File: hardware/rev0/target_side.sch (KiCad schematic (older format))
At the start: 4 parts, among them IC1 ECP5-BGA256, U9 AT86RF215

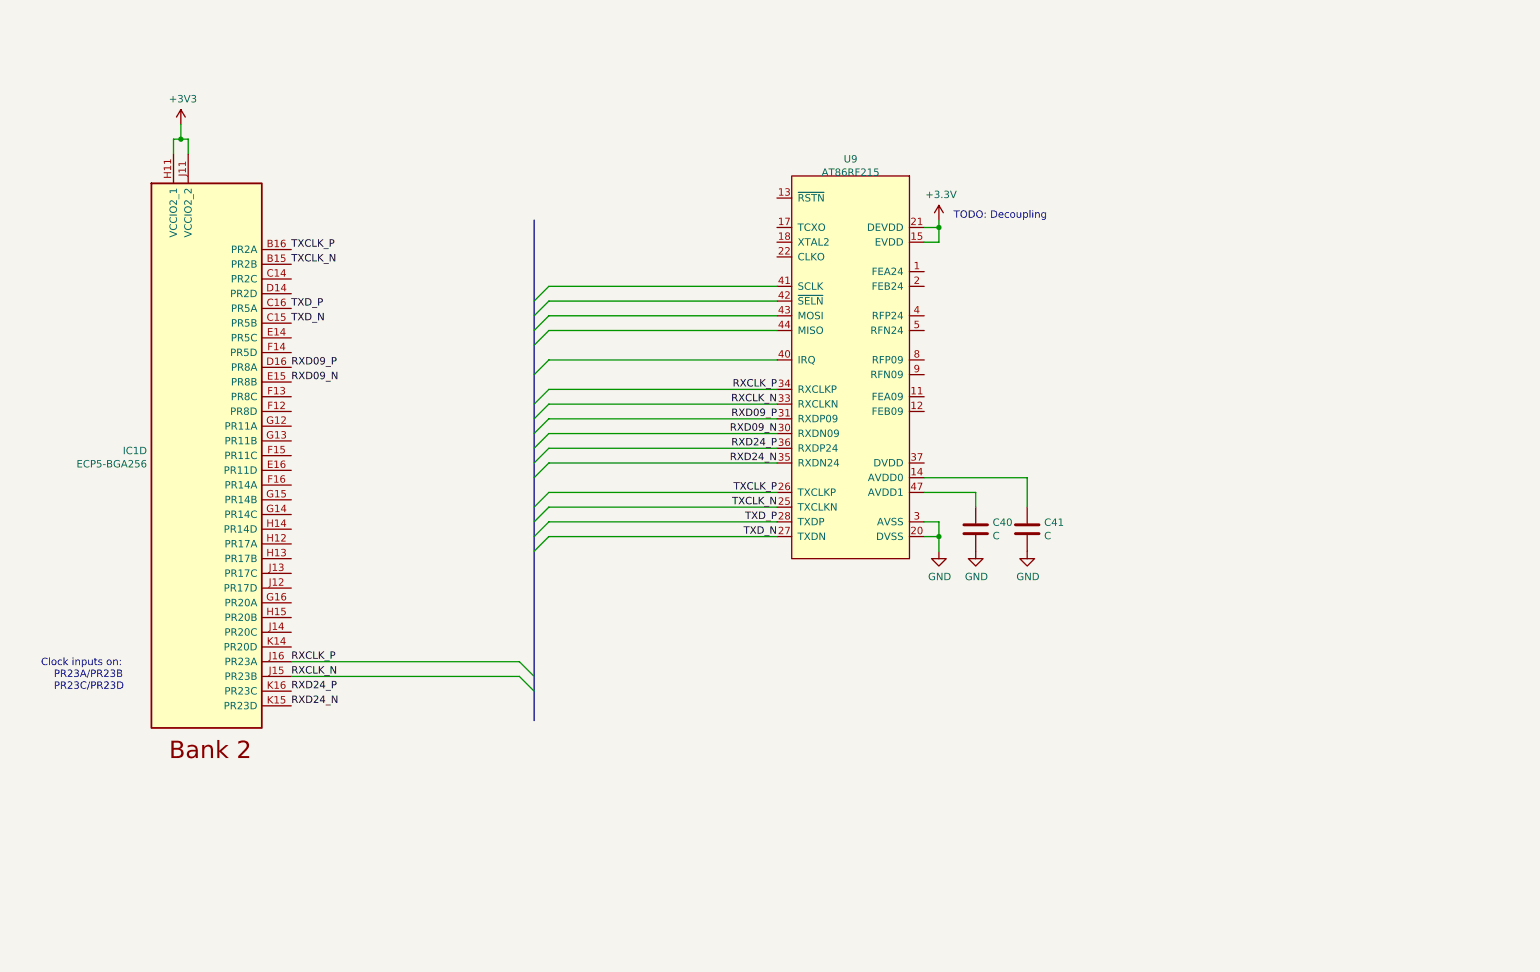
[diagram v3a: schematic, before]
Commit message: Add baluns, matching, TXCO, decoupling
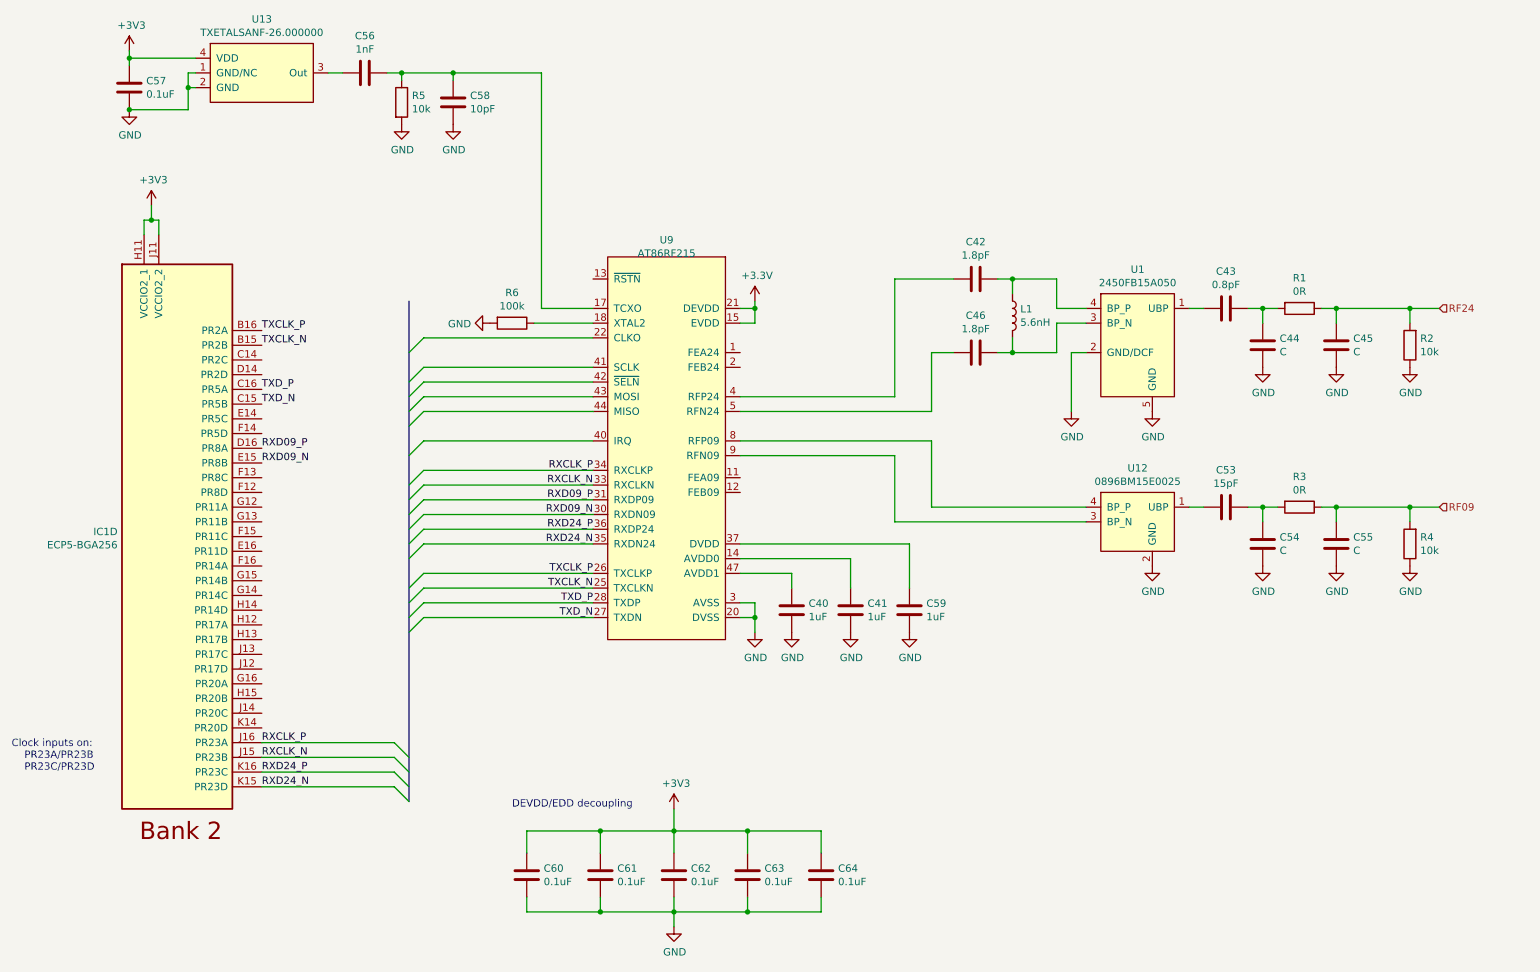
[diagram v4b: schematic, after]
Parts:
- added C42, C46: 1.8pF, Capacitor_SMD:C_0402_1005Metric, symbol Device:C
- added C43: 0.8pF, Capacitor_SMD:C_0402_1005Metric, symbol Device:C
- added C44, C45, C54, C55: C, Capacitor_SMD:C_0402_1005Metric, symbol Device:C
- added C53: 15pF, Capacitor_SMD:C_0402_1005Metric, symbol Device:C
- added C56: 1nF, Capacitor_SMD:C_0402_1005Metric, symbol Device:C
- added C57, C60, C61, C62, C63, C64: 0.1uF, Capacitor_SMD:C_0402_1005Metric, symbol Device:C
- added C58: 10pF, Capacitor_SMD:C_0402_1005Metric, symbol Device:C
- added C59: 1uF, Capacitor_SMD:C_0402_1005Metric, symbol Device:C
- added L1: 5.6nH, Inductor_SMD:L_0402_1005Metric, symbol Device:L
- added R1, R3: 0R, Resistor_SMD:R_0402_1005Metric, symbol Device:R
- added R2, R4, R5: 10k, Resistor_SMD:R_0402_1005Metric, symbol Device:R
- added R6: 100k, Resistor_SMD:R_0402_1005Metric, symbol Device:R
- added U1: 2450FB15A050, amalthea:Filter_Johanson_2x1.25mm, symbol rf:2450FB15A050
- added U12: 0896BM15E0025, amalthea:Filter_Johanson_2x1.25mm, symbol rf:0896BM15E0025
- added U13: TXETALSANF-26.000000, Oscillator:Oscillator_SMD_SeikoEpson_SG8002CE-4Pin_3.2x2.5mm, symbol rf:TXETALSANF-26.000000
- C40, C41: value C -> 1uF; footprint (none) -> Capacitor_SMD:C_0402_1005Metric
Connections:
- net +3V3: now also C57.1, C60.1, C61.1, C62.1, C63.1, C64.1, U13.4 (VDD)
- net AVSS: now also C44.2, C45.2, C54.2, C55.2, C57.2, C58.2, C59.2, C60.2, C61.2, C62.2, C63.2, C64.2, R2.1, R4.1, R5.2, R6.2, U1.2 (GND/DCF), U1.5 (GND), U12.2 (GND), U12.5 (GND), U12.6 (GND), U13.1 (GND/NC), U13.2 (GND)
- net at U9.17 (TCXO): now also C56.1, C58.1, R5.1
- net at U9.18 (XTAL2): now also R6.1
- net at U9.37 (DVDD): now also C59.1
- net at U9.4 (RFP24): now also C42.2
- net at U9.5 (RFN24): now also C46.1
- net at U9.8 (RFP09): now also U12.4 (BP_P)
- net at U9.9 (RFN09): now also U12.3 (BP_N)
- new net: C43.2, U1.1 (UBP)
- new net: C46.2, L1.2, U1.3 (BP_N)
- new net: C42.1, L1.1, U1.4 (BP_P)
- new net: C53.2, U12.1 (UBP)
- new net: C43.1, C44.1, R1.2
- new net: C53.1, C54.1, R3.2
- new net: C56.2, U13.3 (Out)
- new net RF09: C55.1, R3.1, R4.2
- new net RF24: C45.1, R1.1, R2.2
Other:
- note added: "DEVDD/EDD decoupling"
- note removed: "TODO: Decoupling\n"
- moved on the sheet: C40, C41, IC1D, U9

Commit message: Do a bunch of placement
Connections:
- net ~SELN: now reaches IC1.E16 (PR11D)
- net ~SELN: now also U9.42 (~SELN)
- net MOSI: now reaches IC1.F16 (PR14A)
- net MOSI: now also U9.43 (MOSI)
- net MISO: now reaches IC1.G16 (PR20A)
- net MISO: now also U9.44 (MISO)
- net SCLK: now reaches IC1.K14 (PR20D)
- net SCLK: now also U9.41 (SCLK)
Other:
- note added: "TODO: swap 24/09 position to match physical layout"
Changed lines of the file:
@@
 U 1 1 5E8BDF16
 P 5150 3900
-F 0 "U9" H 5150 5315 50  0000 C CNN
-F 1 "AT86RF215" H 5150 5224 50  0000 C CNN
+F 0 "U9" H 5150 5350 50  0000 C CNN
+F 1 "AT86RF215" H 5150 5250 50  0000 C CNN
 F 2 "Package_DFN_QFN:QFN-48-1EP_7x7mm_P0.5mm_EP5.6x5.6mm" H 5150 3650 50  0001 C CNN
 F 3 "" H 5150 3650 50  0001 C CNN
@@
 Wire Wire Line
 	6700 4400 8000 4400
-Text HLabel 10400 4300 2    50   Input ~ 0
-RF09
 $Comp
 L Device:C C42
@@
 	-1   0    0    1
 $EndComp
-Text HLabel 10400 2950 2    50   Input ~ 0
-RF24
 Wire Wire Line
 	9100 2950 9200 2950
@@
 Wire Wire Line
 	5700 6500 6200 6500
+Text Notes 4100 6350 0    50   ~ 0
+DEVDD/EDD decoupling
+Text Label 4650 3350 2    50   ~ 0
+SCLK
+Text Label 4650 3450 2    50   ~ 0
+~SELN
+Text Label 4650 3550 2    50   ~ 0
+MOSI
+Text Label 4650 3650 2    50   ~ 0
+MISO
 Wire Bus Line
 	3400 2900 3400 6300
-Text Notes 4100 6350 0    50   ~ 0
-DEVDD/EDD decoupling
+Text Notes 8550 2500 0    50   ~ 0
+TODO: swap 24/09 position to match physical layout
+Text Label 2400 5800 0    50   ~ 0
+SCLK
+Text Label 2400 4600 0    50   ~ 0
+~SELN
+Text Label 2400 4700 0    50   ~ 0
+MOSI
+Text Label 2400 5500 0    50   ~ 0
+MISO
+Text HLabel 10400 2950 2    50   Input ~ 0
+RF24
+Text HLabel 10400 4300 2    50   Input ~ 0
+RF09
 $EndSCHEMATC

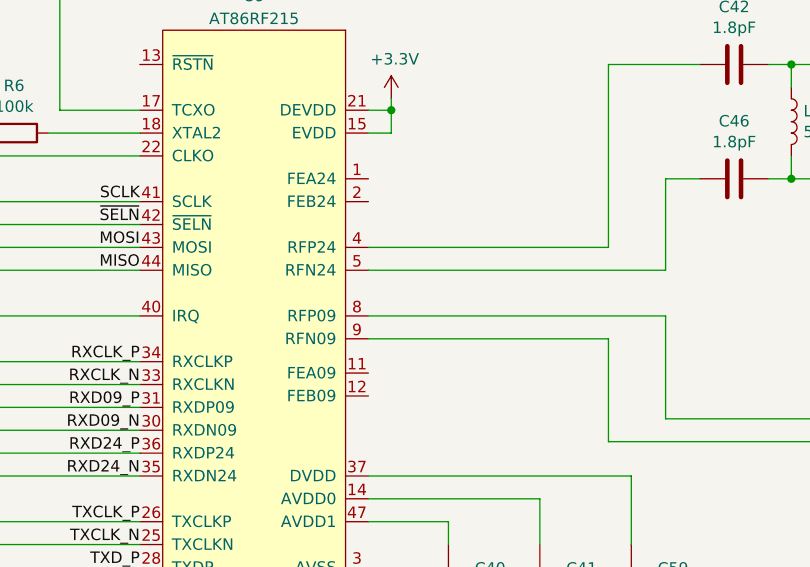
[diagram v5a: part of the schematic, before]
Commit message: Route most of the 'RF215
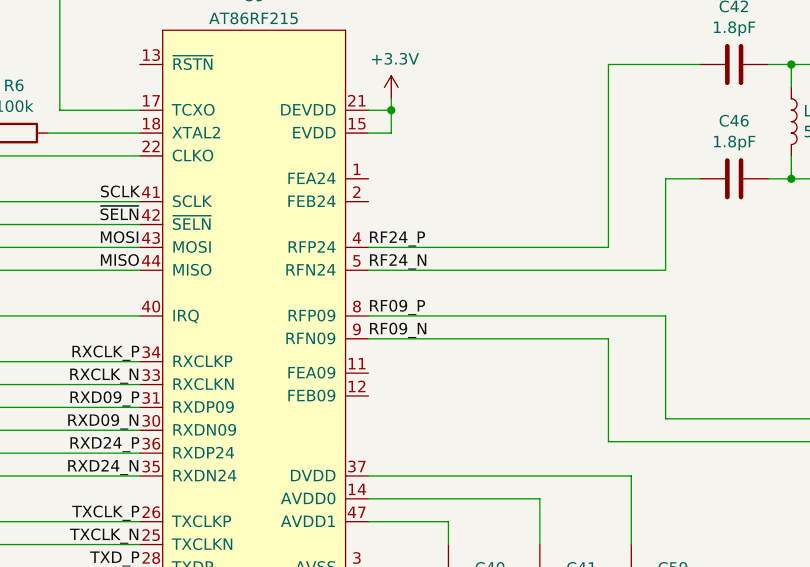
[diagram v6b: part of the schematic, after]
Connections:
- net RF24_P: now reaches C42.2, U9.4 (RFP24)
- net RF24_N: now reaches C46.1, U9.5 (RFN24)
- net RF09_P: now reaches U12.4 (BP_P), U9.8 (RFP09)
- net RF09_N: now reaches U12.3 (BP_N), U9.9 (RFN09)
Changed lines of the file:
@@
 Text HLabel 10400 4300 2    50   Input ~ 0
 RF09
+Text Label 5650 3550 0    50   ~ 0
+RF24_P
+Text Label 5650 3650 0    50   ~ 0
+RF24_N
+Text Label 5650 3850 0    50   ~ 0
+RF09_P
+Text Label 5650 3950 0    50   ~ 0
+RF09_N
 $EndSCHEMATC

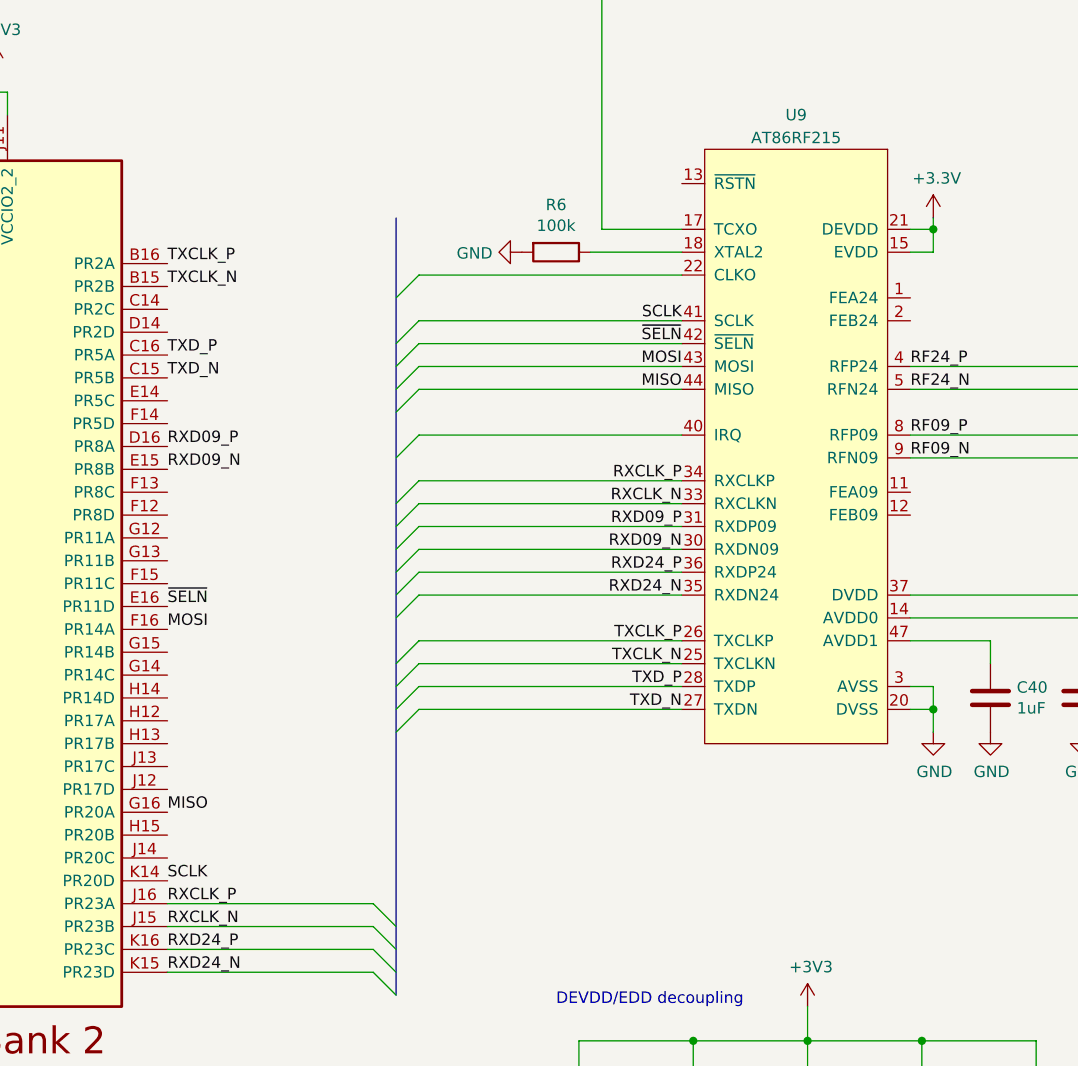
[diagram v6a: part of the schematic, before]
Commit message: Route/NC remaining target signals, ERC & schematic cleanup
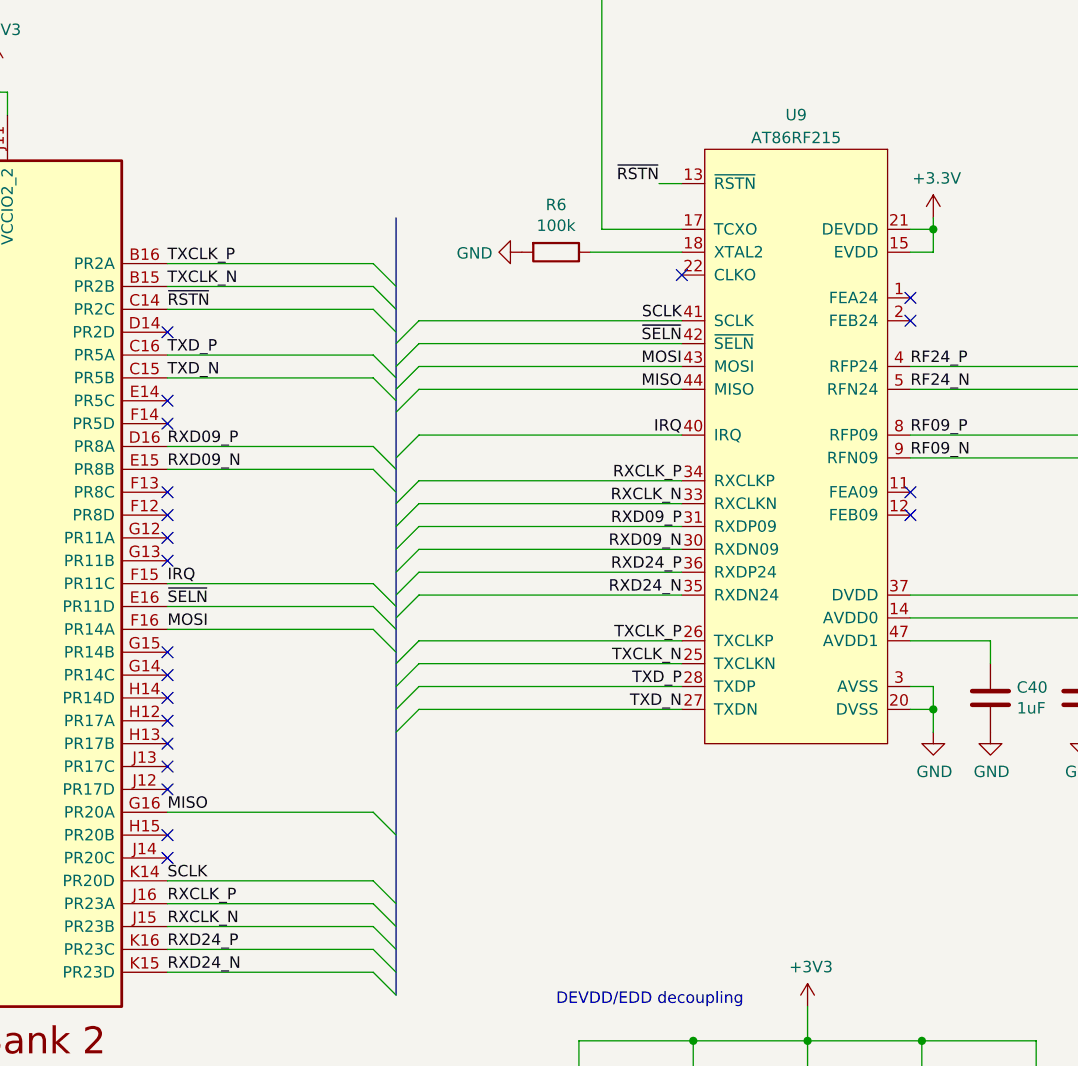
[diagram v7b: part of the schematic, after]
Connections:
- net ~RSTN: now reaches IC1.C14 (PR2C)
- net ~RSTN: now also U9.13 (~RSTN)
- net IRQ: now reaches IC1.F15 (PR11C)
- net IRQ: now also U9.40 (IRQ)
- no-connect marks 0 -> 21
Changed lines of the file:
@@
 Wire Wire Line
 	4250 3050 4650 3050
-Entry Wire Line
-	3400 3250 3500 3150
-Wire Wire Line
-	4650 3150 3500 3150
 $Comp
 L Device:C C59
@@
 Text Label 4650 3650 2    50   ~ 0
 MISO
-Wire Bus Line
-	3400 2900 3400 6300
 Text Notes 8550 2500 0    50   ~ 0
 TODO: swap 24/09 position to match physical layout
@@
 Text Label 5650 3950 0    50   ~ 0
 RF09_N
+NoConn ~ 4650 3150
+Wire Wire Line
+	4550 2750 4650 2750
+Text Label 4650 3850 2    50   ~ 0
+IRQ
+Text Label 2400 4500 0    50   ~ 0
+IRQ
+Text Label 4550 2750 2    50   ~ 0
+~RSTN
+Text Label 2400 3300 0    50   ~ 0
+~RSTN
+NoConn ~ 5650 3250
+NoConn ~ 5650 3350
+NoConn ~ 5650 4100
+NoConn ~ 5650 4200
+NoConn ~ 2400 5600
+NoConn ~ 2400 5700
+NoConn ~ 2400 5300
+NoConn ~ 2400 5400
+NoConn ~ 2400 5200
+NoConn ~ 2400 5100
+NoConn ~ 2400 5000
+NoConn ~ 2400 4900
+NoConn ~ 2400 4800
+NoConn ~ 2400 4300
+NoConn ~ 2400 4200
+NoConn ~ 2400 4100
+NoConn ~ 2400 3800
+NoConn ~ 2400 3700
+NoConn ~ 2400 3400
+NoConn ~ 2400 4400
+Entry Wire Line
+	3300 5800 3400 5900
+Entry Wire Line
+	3300 5500 3400 5600
+Entry Wire Line
+	3300 4700 3400 4800
+Entry Wire Line
+	3300 4600 3400 4700
+Entry Wire Line
+	3300 4500 3400 4600
+Entry Wire Line
+	3300 4000 3400 4100
+Entry Wire Line
+	3300 3900 3400 4000
+Entry Wire Line
+	3300 3600 3400 3700
+Entry Wire Line
+	3300 3500 3400 3600
+Entry Wire Line
+	3300 3300 3400 3400
+Entry Wire Line
+	3300 3200 3400 3300
+Entry Wire Line
+	3300 3100 3400 3200
+Wire Wire Line
+	2400 3100 3300 3100
+Wire Wire Line
+	3300 3200 2400 3200
+Wire Wire Line
+	2400 3300 3300 3300
+Wire Wire Line
+	3300 3500 2400 3500
+Wire Wire Line
+	2400 3600 3300 3600
+Wire Wire Line
+	2400 3900 3300 3900
+Wire Wire Line
+	3300 4000 2400 4000
+Wire Wire Line
+	2400 4500 3300 4500
+Wire Wire Line
+	3300 4600 2400 4600
+Wire Wire Line
+	2400 4700 3300 4700
+Wire Wire Line
+	3300 5500 2400 5500
+Wire Wire Line
+	2400 5800 3300 5800
+Wire Bus Line
+	3400 2900 3400 6300
 $EndSCHEMATC
